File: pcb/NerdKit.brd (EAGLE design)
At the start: 148.3 x 69.8 mm, 31 parts, among them U2 ARDUINOR3-PINSONLY

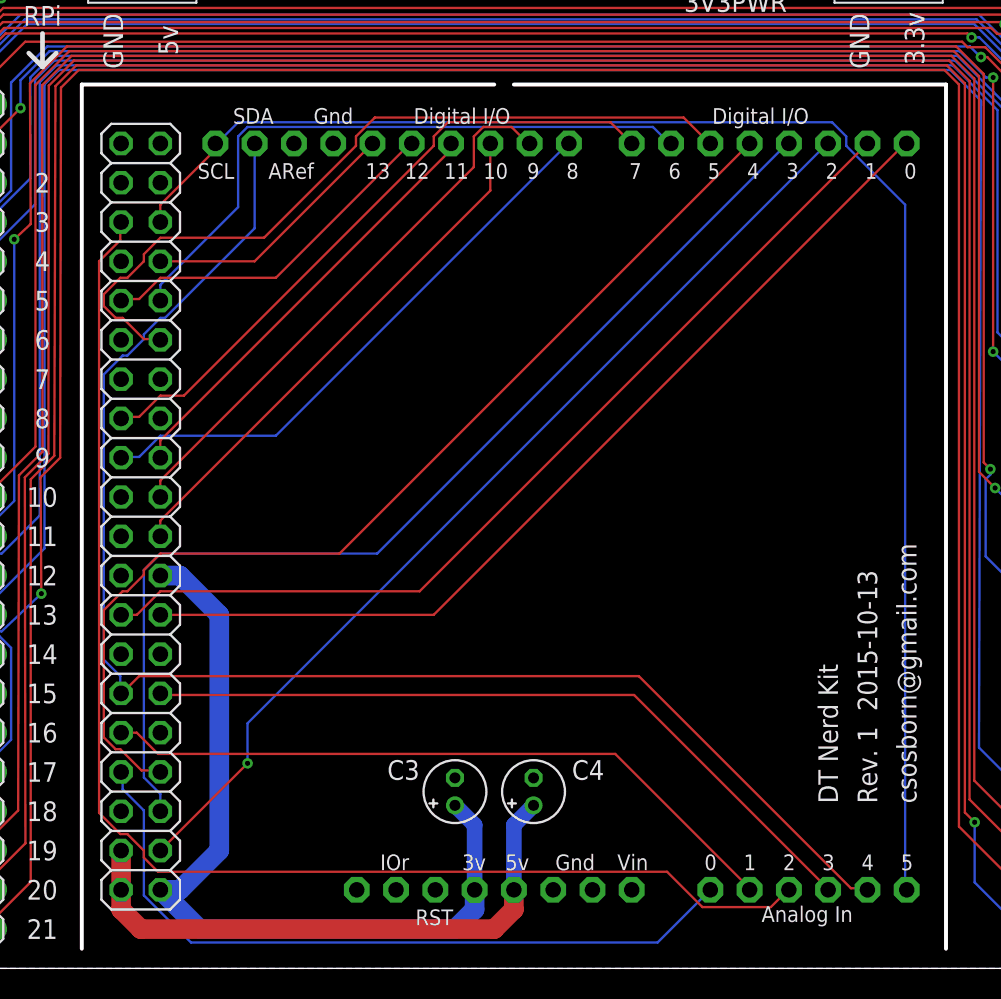
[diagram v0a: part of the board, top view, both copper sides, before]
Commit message: Corrected the header orientation on the Arduino shield adapter card.
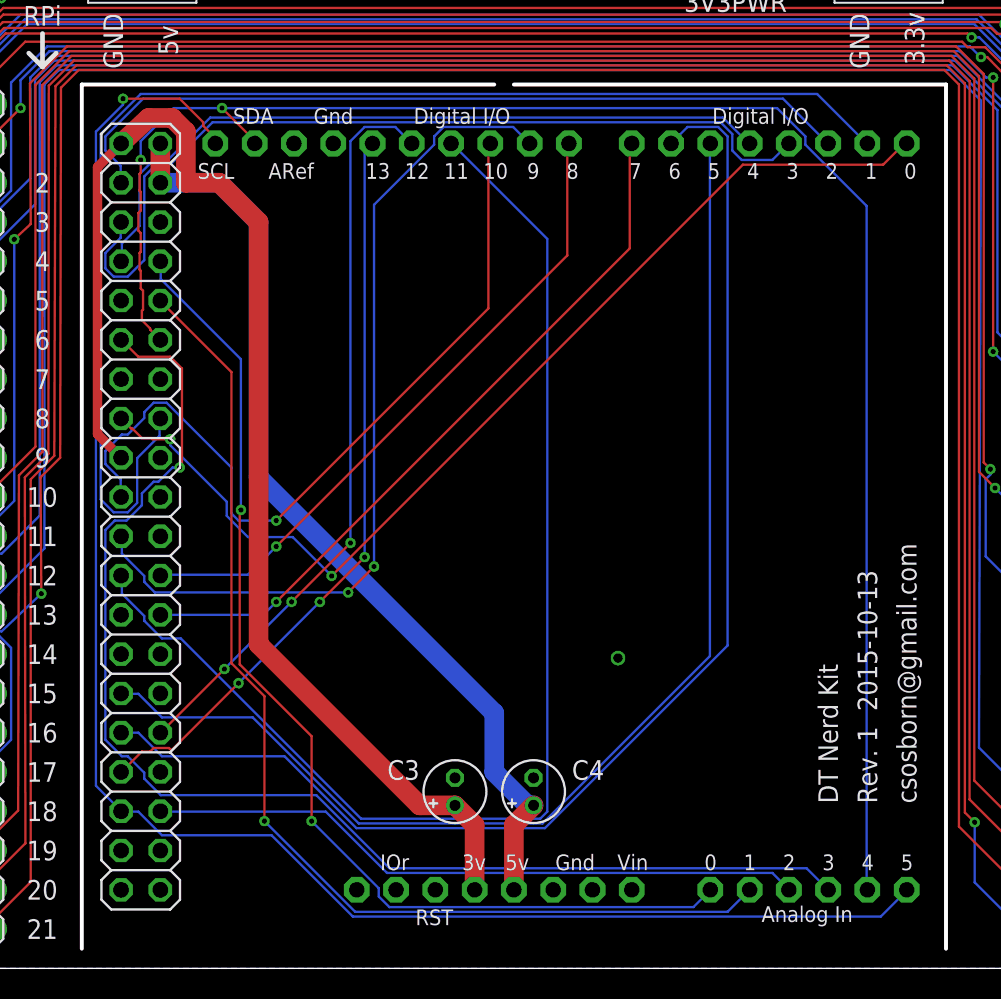
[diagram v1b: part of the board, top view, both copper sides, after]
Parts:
- turned ARDUINOIO to 270 degrees
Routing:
- net AR11: track 28.1 -> 80.9 mm
- net ARA2: track 86.6 -> 42.8 mm
- net AR06: track 41.4 -> 83.9 mm
- net ARA3: track 48.5 -> 82.6 mm, vias 0 -> 1
- net AR_3V3: track 54.1 -> 86.1 mm
- net AR13: track 16.9 -> 48.6 mm, vias 0 -> 3
- net AR05: track 50.6 -> 79.2 mm
- net ARA1: track 44.9 -> 70.8 mm, vias 0 -> 1
- net AR12: track 23.0 -> 48.1 mm, vias 0 -> 3
- net AR01: track 60.9 -> 84.6 mm
- net AR_5V: track 37.5 -> 61.2 mm
- net ARA0: track 47.9 -> 69.2 mm, vias 0 -> 2
- net AR09: track 36.0 -> 55.7 mm, vias 0 -> 2
- net AR04: track 67.3 -> 47.8 mm
- net ARA4: track 94.9 -> 111.9 mm, vias 0 -> 2
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
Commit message: Corrected the header orientation on the secondary LED card.
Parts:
- turned ARDUINOIO1 to 270 degrees
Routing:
- net LED_SCK: track 26.5 -> 51.6 mm
- net LED_VCC: track 183.1 -> 176.3 mm
- net LED_MOSI: track 42.1 -> 38.7 mm
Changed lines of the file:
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@@
 <element name="LED9" library="osborn" package="RGBLED5050" value="RGBLED5050" x="18.5166" y="33.909" rot="R72"/>
 <element name="LED10" library="osborn" package="RGBLED5050" value="RGBLED5050" x="24.0538" y="41.529" rot="R36"/>
-<element name="ARDUINOIO1" library="pinhead" package="2X20" value="" x="3.81" y="29.21" smashed="yes" rot="R90">
-<attribute name="VALUE" x="8.255" y="3.81" size="1.27" layer="27" rot="R90"/>
+<element name="ARDUINOIO1" library="pinhead" package="2X20" value="" x="3.81" y="29.21" smashed="yes" rot="R270">
+<attribute name="VALUE" x="-0.635" y="54.61" size="1.27" layer="27" rot="R270"/>
 </element>
 </elements>
@@
 <contactref element="ARDUINOIO1" pad="34"/>
 <via x="103.251" y="20.066" extent="1-16" drill="0.6"/>
-<wire x1="73.66" y1="48.26" x2="71.12" y2="43.18" width="0" layer="19" extent="1-1"/>
+<wire x1="73.66" y1="48.26" x2="73.5838" y2="48.183784375" width="0.1524" layer="1"/>
+<wire x1="73.5838" y1="48.183784375" x2="71.12" y2="43.18" width="0" layer="19" extent="1-1"/>
 </signal>
 <signal name="GNDBREAK">
@@
 <wire x1="19.515359375" y1="26.938440625" x2="33.02" y2="29.21" width="1.27" layer="1"/>
 <wire x1="20.751428125" y1="35.28578125" x2="33.02" y2="29.21" width="1.27" layer="1"/>
-<wire x1="2.54" y1="7.62" x2="2.54" y2="5.08" width="1.27" layer="16"/>
-<wire x1="7.62" y1="2.54" x2="33.02" y2="29.21" width="1.27" layer="16"/>
-<wire x1="7.62" y1="2.54" x2="3.81" y2="2.54" width="1.27" layer="16"/>
-<wire x1="3.81" y1="2.54" x2="2.54" y2="3.81" width="1.27" layer="16"/>
-<wire x1="2.54" y1="3.81" x2="2.54" y2="5.08" width="1.27" layer="16"/>
+<wire x1="5.08" y1="53.34" x2="5.08" y2="50.8" width="1.27" layer="16"/>
+<wire x1="5.08" y1="50.8" x2="11.43" y2="50.8" width="1.27" layer="16"/>
+<wire x1="11.43" y1="50.8" x2="33.02" y2="29.21" width="1.27" layer="16"/>
 </signal>
 <signal name="LED_SCK">
 <contactref element="ARDUINOIO1" pad="33"/>
 <contactref element="LED1" pad="2"/>
-<wire x1="5.08" y1="45.72" x2="27.94" y2="45.72" width="0.3048" layer="1"/>
-<wire x1="27.94" y1="45.72" x2="29.21" y2="44.45" width="0.3048" layer="1"/>
-<wire x1="29.21" y1="44.45" x2="31.02" y2="44.45" width="0.3048" layer="1"/>
+<wire x1="29.21" y1="45.72" x2="30.48" y2="44.45" width="0.1524" layer="1"/>
+<wire x1="23.495" y1="45.72" x2="29.21" y2="45.72" width="0.1524" layer="1"/>
+<wire x1="6.985" y1="29.21" x2="23.495" y2="45.72" width="0.1524" layer="1"/>
+<wire x1="6.985" y1="13.97" x2="6.985" y2="29.21" width="0.1524" layer="1"/>
+<wire x1="3.81" y1="13.97" x2="6.985" y2="13.97" width="0.1524" layer="1"/>
+<wire x1="2.54" y1="12.7" x2="3.81" y2="13.97" width="0.1524" layer="1"/>
+<wire x1="30.48" y1="44.45" x2="31.02" y2="44.45" width="0.1524" layer="1"/>
 </signal>
 <signal name="LED_MOSI">
 <contactref element="ARDUINOIO1" pad="23"/>
 <contactref element="LED1" pad="1"/>
-<wire x1="5.08" y1="33.02" x2="3.81" y2="34.29" width="0.3048" layer="1"/>
-<wire x1="3.81" y1="34.29" x2="3.81" y2="46.99" width="0.3048" layer="1"/>
-<wire x1="3.81" y1="46.99" x2="30.226" y2="46.99" width="0.3048" layer="1"/>
-<wire x1="30.226" y1="46.99" x2="31.02" y2="46.15" width="0.3048" layer="1"/>
+<wire x1="23.495" y1="46.355" x2="30.48" y2="46.355" width="0.1524" layer="1"/>
+<wire x1="6.35" y1="29.21" x2="23.495" y2="46.355" width="0.1524" layer="1"/>
+<wire x1="6.35" y1="26.67" x2="6.35" y2="29.21" width="0.1524" layer="1"/>
+<wire x1="3.81" y1="26.67" x2="6.35" y2="26.67" width="0.1524" layer="1"/>
+<wire x1="2.54" y1="25.4" x2="3.81" y2="26.67" width="0.1524" layer="1"/>
+<wire x1="30.48" y1="46.355" x2="31.02" y2="46.15" width="0.1524" layer="1"/>
 </signal>
 <signal name="LED_MISO">

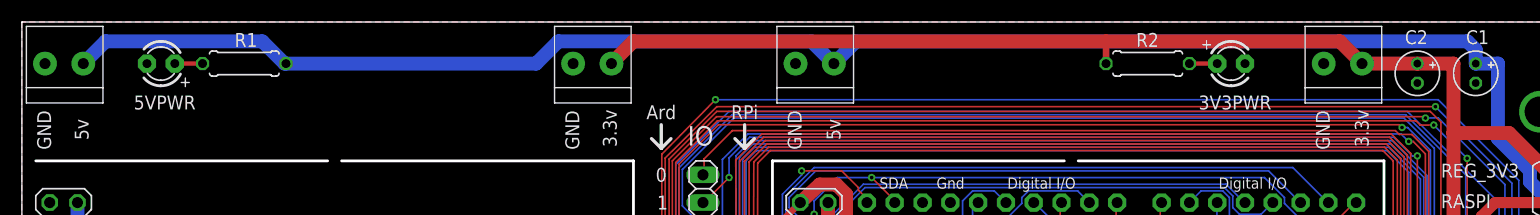
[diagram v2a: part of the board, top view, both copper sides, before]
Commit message: Adjusted power terminal blocks and associated components 0.1" inboard.
Fixes #2.
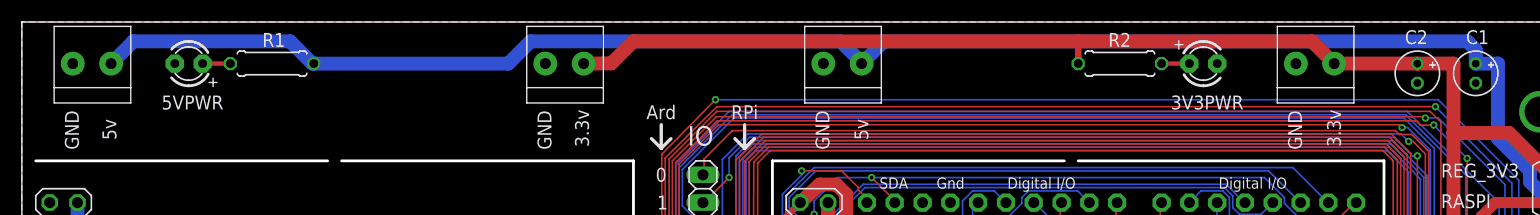
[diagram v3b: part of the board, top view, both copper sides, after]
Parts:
- moved PB2_TB_3V3 2.54 mm to (118.1, 66.0)
- moved PB2_TB_5V 2.54 mm to (74.9, 66.0)
- moved R2 2.54 mm to (100.3, 66.0)
- moved 5VPWR 2.54 mm to (15.2, 66.0)
- moved PB1_TB_5V 2.54 mm to (6.35, 66.0)
- moved PB1_TB_3V3 2.54 mm to (49.5, 66.0)
- moved R1 2.54 mm to (22.9, 66.0)
- moved 3V3PWR 2.54 mm to (108.0, 66.0)
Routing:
- net 3V3: track 128.9 -> 131.4 mm
- net 5V: track 166.0 -> 163.5 mm
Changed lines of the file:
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@@
 <wire x1="68.58" y1="57.15" x2="68.58" y2="1.27" width="0.254" layer="20"/>
 <wire x1="124.46" y1="57.15" x2="124.46" y2="1.27" width="0.254" layer="20"/>
-<text x="2.667" y="58.166" size="1.27" layer="25" rot="R90">GND</text>
-<text x="50.927" y="58.166" size="1.27" layer="25" rot="R90">GND</text>
-<text x="71.247" y="58.166" size="1.27" layer="25" rot="R90">GND</text>
-<text x="119.507" y="58.166" size="1.27" layer="25" rot="R90">GND</text>
-<text x="6.096" y="59.055" size="1.27" layer="25" rot="R90">5v</text>
-<text x="74.803" y="59.055" size="1.27" layer="25" rot="R90">5v</text>
-<text x="54.356" y="58.42" size="1.27" layer="25" rot="R90">3.3v</text>
-<text x="123.063" y="58.42" size="1.27" layer="25" rot="R90">3.3v</text>
+<text x="5.207" y="58.166" size="1.27" layer="25" rot="R90">GND</text>
+<text x="48.387" y="58.166" size="1.27" layer="25" rot="R90">GND</text>
+<text x="73.787" y="58.166" size="1.27" layer="25" rot="R90">GND</text>
+<text x="116.967" y="58.166" size="1.27" layer="25" rot="R90">GND</text>
+<text x="8.636" y="59.055" size="1.27" layer="25" rot="R90">5v</text>
+<text x="77.343" y="59.055" size="1.27" layer="25" rot="R90">5v</text>
+<text x="51.816" y="58.42" size="1.27" layer="25" rot="R90">3.3v</text>
+<text x="120.523" y="58.42" size="1.27" layer="25" rot="R90">3.3v</text>
 <text x="60.833" y="58.547" size="1.778" layer="25">IO</text>
 <text x="58.42" y="60.96" size="1.27" layer="25" align="bottom-center">Ard</text>
@@
 <attribute name="VALUE" x="125.73" y="62.992" size="1.27" layer="27" ratio="10" rot="R270"/>
 </element>
-<element name="PB1_TB_3V3" library="adafruit" package="1X2-3.5MM" value="1X2-3.5MM" x="52.07" y="66.04" smashed="yes"/>
-<element name="PB1_TB_5V" library="adafruit" package="1X2-3.5MM" value="1X2-3.5MM" x="3.81" y="66.04" smashed="yes"/>
-<element name="PB2_TB_3V3" library="adafruit" package="1X2-3.5MM" value="1X2-3.5MM" x="120.65" y="66.04" smashed="yes"/>
-<element name="PB2_TB_5V" library="adafruit" package="1X2-3.5MM" value="1X2-3.5MM" x="72.39" y="66.04" smashed="yes"/>
+<element name="PB1_TB_3V3" library="adafruit" package="1X2-3.5MM" value="1X2-3.5MM" x="49.53" y="66.04" smashed="yes"/>
+<element name="PB1_TB_5V" library="adafruit" package="1X2-3.5MM" value="1X2-3.5MM" x="6.35" y="66.04" smashed="yes"/>
+<element name="PB2_TB_3V3" library="adafruit" package="1X2-3.5MM" value="1X2-3.5MM" x="118.11" y="66.04" smashed="yes"/>
+<element name="PB2_TB_5V" library="adafruit" package="1X2-3.5MM" value="1X2-3.5MM" x="74.93" y="66.04" smashed="yes"/>
 <element name="REG_3V3" library="adafruit" package="TO92" value="L4931" x="139.7" y="54.61" smashed="yes" rot="R270">
 <attribute name="NAME" x="129.667" y="55.626" size="1.27" layer="25" ratio="10"/>
@@
 <attribute name="VALUE" x="137.16" y="72.39" size="1.27" layer="27" rot="R270"/>
 </element>
-<element name="5VPWR" library="adafruit" package="LED3MM" value="RED" x="12.7" y="66.04" smashed="yes" rot="R180">
-<attribute name="NAME" x="15.875" y="63.119" size="1.27" layer="25" ratio="10" rot="R180"/>
-<attribute name="VALUE" x="10.795" y="67.691" size="1.27" layer="27" ratio="10" rot="R180"/>
-</element>
-<element name="3V3PWR" library="adafruit" package="LED3MM" value="RED" x="110.49" y="66.04" smashed="yes">
-<attribute name="NAME" x="114.173" y="63.119" size="1.27" layer="25" ratio="10" rot="R180"/>
-<attribute name="VALUE" x="112.395" y="64.389" size="1.27" layer="27" ratio="10"/>
-</element>
-<element name="R1" library="adafruit" package="0207/7" value="" x="20.32" y="66.04" smashed="yes">
-<attribute name="NAME" x="19.431" y="67.564" size="1.27" layer="25" ratio="10"/>
-<attribute name="VALUE" x="18.034" y="65.4812" size="1.27" layer="27" ratio="10"/>
-</element>
-<element name="R2" library="adafruit" package="0207/7" value="" x="102.87" y="66.04" smashed="yes" rot="R180">
-<attribute name="NAME" x="103.886" y="68.834" size="1.27" layer="25" ratio="10" rot="R180"/>
-<attribute name="VALUE" x="105.156" y="66.5988" size="1.27" layer="27" ratio="10" rot="R180"/>
+<element name="5VPWR" library="adafruit" package="LED3MM" value="RED" x="15.24" y="66.04" smashed="yes" rot="R180">
+<attribute name="NAME" x="18.415" y="63.119" size="1.27" layer="25" ratio="10" rot="R180"/>
+<attribute name="VALUE" x="13.335" y="67.691" size="1.27" layer="27" ratio="10" rot="R180"/>
+</element>
+<element name="3V3PWR" library="adafruit" package="LED3MM" value="RED" x="107.95" y="66.04" smashed="yes">
+<attribute name="NAME" x="111.633" y="63.119" size="1.27" layer="25" ratio="10" rot="R180"/>
+<attribute name="VALUE" x="109.855" y="64.389" size="1.27" layer="27" ratio="10"/>
+</element>
+<element name="R1" library="adafruit" package="0207/7" value="" x="22.86" y="66.04" smashed="yes">
+<attribute name="NAME" x="21.971" y="67.564" size="1.27" layer="25" ratio="10"/>
+<attribute name="VALUE" x="20.574" y="65.4812" size="1.27" layer="27" ratio="10"/>
+</element>
+<element name="R2" library="adafruit" package="0207/7" value="" x="100.33" y="66.04" smashed="yes" rot="R180">
+<attribute name="NAME" x="101.346" y="68.834" size="1.27" layer="25" ratio="10" rot="R180"/>
+<attribute name="VALUE" x="102.616" y="66.5988" size="1.27" layer="27" ratio="10" rot="R180"/>
 </element>
 <element name="RASPI+" library="pinhead" package="2X06" value="" x="132.08" y="8.89" smashed="yes" rot="R270">
@@
 <contactref element="PB2_TB_3V3" pad="1"/>
 <wire x1="130.81" y1="66.04" x2="127.508" y2="66.04" width="1.27" layer="1"/>
-<wire x1="127.508" y1="66.04" x2="122.45" y2="66.04" width="1.27" layer="1"/>
-<wire x1="122.45" y1="66.04" x2="120.418" y2="68.072" width="1.27" layer="1"/>
-<wire x1="120.418" y1="68.072" x2="99.06" y2="68.072" width="1.27" layer="1"/>
-<wire x1="99.06" y1="68.072" x2="55.88" y2="68.072" width="1.27" layer="1"/>
+<wire x1="127.508" y1="66.04" x2="119.91" y2="66.04" width="1.27" layer="1"/>
+<wire x1="119.91" y1="66.04" x2="117.878" y2="68.072" width="1.27" layer="1"/>
+<wire x1="117.878" y1="68.072" x2="96.52" y2="68.072" width="1.27" layer="1"/>
+<wire x1="96.52" y1="68.072" x2="55.88" y2="68.072" width="1.27" layer="1"/>
 <wire x1="55.88" y1="68.072" x2="53.87" y2="66.062" width="1.27" layer="1"/>
-<wire x1="53.87" y1="66.062" x2="53.87" y2="66.04" width="1.27" layer="1"/>
-<wire x1="99.06" y1="66.04" x2="99.06" y2="68.072" width="0.6096" layer="1"/>
+<wire x1="53.87" y1="66.062" x2="51.33" y2="66.04" width="1.27" layer="1"/>
+<wire x1="96.52" y1="66.04" x2="96.52" y2="68.072" width="0.6096" layer="1"/>
 <contactref element="RASPI" pad="1"/>
 <contactref element="RASPI" pad="17"/>
@@
 <contactref element="PB1_TB_5V" pad="1"/>
 <contactref element="PB2_TB_5V" pad="1"/>
-<wire x1="5.61" y1="66.04" x2="7.642" y2="68.072" width="1.27" layer="16"/>
-<wire x1="49.022" y1="68.072" x2="72.136" y2="68.072" width="1.27" layer="16"/>
-<wire x1="72.136" y1="68.072" x2="74.168" y2="66.04" width="1.27" layer="16"/>
-<wire x1="74.168" y1="66.04" x2="74.19" y2="66.04" width="1.27" layer="16"/>
-<wire x1="76.2" y1="68.072" x2="132.08" y2="68.072" width="1.27" layer="16"/>
-<wire x1="74.19" y1="66.04" x2="76.2" y2="68.05" width="1.27" layer="16"/>
-<wire x1="76.2" y1="68.05" x2="76.2" y2="68.072" width="1.27" layer="16"/>
-<wire x1="7.642" y1="68.072" x2="21.971" y2="68.072" width="1.27" layer="16"/>
-<wire x1="21.971" y1="68.072" x2="24.003" y2="66.04" width="1.27" layer="16"/>
-<wire x1="24.003" y1="66.04" x2="24.13" y2="66.04" width="1.27" layer="16"/>
-<wire x1="24.13" y1="66.04" x2="46.99" y2="66.04" width="1.27" layer="16"/>
-<wire x1="46.99" y1="66.04" x2="49.022" y2="68.072" width="1.27" layer="16"/>
+<wire x1="8.15" y1="66.04" x2="10.182" y2="68.072" width="1.27" layer="16"/>
+<wire x1="46.482" y1="68.072" x2="74.803" y2="68.072" width="1.27" layer="16"/>
+<wire x1="78.74" y1="68.072" x2="132.08" y2="68.072" width="1.27" layer="16"/>
+<wire x1="10.182" y1="68.072" x2="24.511" y2="68.072" width="1.27" layer="16"/>
+<wire x1="24.511" y1="68.072" x2="26.543" y2="66.04" width="1.27" layer="16"/>
+<wire x1="26.543" y1="66.04" x2="26.67" y2="66.04" width="1.27" layer="16"/>
 <contactref element="RASPI" pad="2"/>
 <contactref element="RASPI" pad="4"/>
@@
 <wire x1="139.7" y1="48.26" x2="139.7" y2="53.34" width="1.27" layer="16"/>
 <wire x1="133.35" y1="50.8" x2="133.35" y2="48.26" width="1.016" layer="1"/>
+<wire x1="26.67" y1="66.04" x2="44.45" y2="66.04" width="1.27" layer="16"/>
+<wire x1="44.45" y1="66.04" x2="46.482" y2="68.072" width="1.27" layer="16"/>
+<wire x1="76.73" y1="66.04" x2="78.74" y2="68.05" width="1.27" layer="16"/>
+<wire x1="78.74" y1="68.05" x2="78.74" y2="68.072" width="1.27" layer="16"/>
+<wire x1="74.803" y1="68.072" x2="76.73" y2="66.145" width="1.27" layer="16"/>
+<wire x1="76.73" y1="66.145" x2="76.73" y2="66.04" width="1.27" layer="16"/>
 </signal>
 <signal name="GND">
@@
 <contactref element="PB2_TB_5V" pad="2"/>
 <contactref element="PB2_TB_3V3" pad="2"/>
-<wire x1="50.37" y1="66.04" x2="50.292" y2="65.962" width="1.27" layer="16"/>
-<wire x1="50.292" y1="66.04" x2="50.37" y2="66.04" width="1.27" layer="16"/>
-<wire x1="70.739" y1="66.04" x2="70.69" y2="66.04" width="1.27" layer="16"/>
 <contactref element="RASPI" pad="9"/>
 <contactref element="RASPI" pad="25"/>
@@
 <contactref element="R1" pad="1"/>
 <contactref element="5VPWR" pad="A"/>
-<wire x1="13.97" y1="66.04" x2="16.51" y2="66.04" width="0.4064" layer="1"/>
+<wire x1="16.51" y1="66.04" x2="19.05" y2="66.04" width="0.4064" layer="1"/>
 </signal>
 <signal name="N$1">
 <contactref element="R2" pad="1"/>
 <contactref element="3V3PWR" pad="A"/>
-<wire x1="109.22" y1="66.04" x2="106.68" y2="66.04" width="0.4064" layer="1"/>
+<wire x1="106.68" y1="66.04" x2="104.14" y2="66.04" width="0.4064" layer="1"/>
 </signal>
 <signal name="GPIO03">

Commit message: Corrected schematic error on LED6 ground pin and adjusted copper pour.
Fixes #7.
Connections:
- net GND: now also LED6.3
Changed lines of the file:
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@@
 <via x="103.251" y="20.066" extent="1-16" drill="0.6"/>
 <wire x1="73.66" y1="48.26" x2="73.5838" y2="48.183784375" width="0.1524" layer="1"/>
+<contactref element="LED6" pad="3"/>
 <wire x1="73.5838" y1="48.183784375" x2="71.12" y2="43.18" width="0" layer="19" extent="1-1"/>
 </signal>
